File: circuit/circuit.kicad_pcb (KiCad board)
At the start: 2 copper layers, 25 parts, among them J1 JST-PH_2_RA, J2 CONN_02X03, U1 SK812, U2 MIC5504-3.3YM5, U3 ADXL345, U4 ATmega328-AU, Y1 Crystal_SMD

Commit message: modified schematic and layout:
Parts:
- removed J2: CONN_02X03, rocketry:Pin_Header_Straight_2x03
- added C8: C_1uF, footprints:C_0805_OEM, F.Cu at (187.8, 85.4)
- added C9: C_0.1uF, footprints:C_0805_OEM, F.Cu at (185.7, 85.4)
- added U5: USB_MicroB, Connectors_USB:USB_Micro-B_Molex-105017-0001, F.Cu at (189.3, 76.4)
- C2: value C_30pF -> C_10uF; footprint rocketry:C_0805_OEM -> footprints:C_0805_OEM
- C3: value C_30pF -> C_100uF; footprint rocketry:C_0805_OEM -> footprints:C_0805_OEM
- U2: value MIC5504-3.3YM5 -> LM1117-3.3; footprint rocketry:SOT-23-5_OEM -> TO_SOT_Packages_SMD:SOT-223
- moved D3 127.9 mm to (211.5, 80.8), turned to 90 degrees
- moved D2 123.2 mm to (205.2, 110.9), turned to 90 degrees
- moved D1 118.3 mm to (197.8, 76.2), turned to 180 degrees
- moved C2 117.6 mm to (209.5, 86.2), turned to 270 degrees
- moved C4 117.3 mm to (207.6, 98.8), turned to 90 degrees
- moved R3 114.5 mm to (211.6, 84.5), turned to 90 degrees
- moved R1 112.5 mm to (207.2, 111.3), turned to 270 degrees
- moved U1 111.4 mm to (188.0, 110.4), turned to 90 degrees
- moved U3 110.8 mm to (190.7, 86.4)
- moved C7 110.5 mm to (204.1, 102.6), turned to 90 degrees
- moved R2 109.5 mm to (197.8, 78.3), turned to 180 degrees
- moved C5 102.1 mm to (205.0, 95.4)
- moved C3 101.6 mm to (203.8, 92.5)
- moved Y1 101.4 mm to (204.9, 98.6), turned to 90 degrees
- moved R5 101.0 mm to (188.8, 106.0)
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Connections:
- C1 pad 1: GND -> VCC
- C3 pad 1: GND -> VCC
- C4 pad 2: Net-(C4-Pad2) -> GND
- C5 pad 2: Net-(C4-Pad2) -> GND
- C7 pad 2: GND -> VCC
- D3 pad 2: GND -> VCC
- R6 pad 2: GND -> VCC
- R7 pad 1: GND -> VCC
- SD1 pad 4: GND -> VCC
- U1 pad 1: GND -> VCC
- U2 pad 1: /Battery+ -> GND
- U2 pad 2: GND -> VCC
- U2 pad 4: Net-(U2-Pad4) -> VCC
- U3 pad 1: GND -> VCC
- U3 pad 6: GND -> VCC
- U4 pad 1: /INT2 -> Net-(U4-Pad1)
- U4 pad 11: Net-(U4-Pad11) -> /SD_Select
- U4 pad 12: /P_LED_1 -> /cardIN
- U4 pad 13: /cardIN -> /INT2
- U4 pad 14: Net-(U4-Pad14) -> /INT1
- U4 pad 25: /SD_Select -> Net-(U4-Pad25)
- U4 pad 27: Net-(U4-Pad27) -> /P_LED_1
- U4 pad 32: /INT1 -> Net-(U4-Pad32)
- U4 pad 4: GND -> VCC
- U4 pad 6: GND -> VCC
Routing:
- net GND: track 0.00 -> 66.0 mm, vias 0 -> 19
- net VCC: track 0.00 -> 64.5 mm, vias 0 -> 8
- net /miso: track 0.00 -> 33.8 mm, vias 0 -> 1
- net /mosi: track 0.00 -> 33.0 mm, vias 0 -> 6
- net /sck: track 0.00 -> 22.9 mm, vias 0 -> 3
- net /SD_Select: track 0.00 -> 19.8 mm, vias 0 -> 3
- net /Slave_Select: track 0.00 -> 18.8 mm
- net /P_LED_1: track 0.00 -> 12.6 mm
- net /INT2: track 0.00 -> 12.1 mm, vias 0 -> 2
- net /INT1: track 0.00 -> 10.6 mm, vias 0 -> 2
- net /Neopix: track 0.00 -> 7.33 mm
- net /Battery+: track 0.00 -> 5.59 mm
- net Net-(C4-Pad1): track 0.00 -> 4.82 mm
- net Net-(C6-Pad1): track 0.00 -> 3.94 mm
- net /cardIN: track 0.00 -> 2.79 mm
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- added copper zone on B.Cu, net GND
- added copper zone on F.Cu, net GND
- added copper zone on F.Cu, net VCC
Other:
- board outline added: 30 x 40 mm
- net class Default: clearance 0.2 -> 0.1524; trace_width 0.25 -> 0.1524; via_dia 0.8 -> 0.6096; via_drill 0.4 -> 0.3048
- rule trace_clearance: 0.2 -> 0.1524
- rule trace_min: 0.2 -> 0.1524
- rule via_min_drill: 0.3 -> 0.3048
- rule via_min_size: 0.4 -> 0.6096
- board text added: "PLUG IN SD"

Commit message: did some more work on the layout. added some graphics
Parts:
- added G***: LOGO, rocketry:pigeon, B.Cu at (198.4, 102.5)
- moved R4 0.55 mm to (197.5, 92.9)
- renumbered U5 to J5
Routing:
- net VCC: track 64.5 -> 128.9 mm, vias 8 -> 18
- net /RESET: track 2.37 -> 41.0 mm, vias 0 -> 2
- net /cardIN: track 2.79 -> 22.7 mm, vias 0 -> 3
- net GND: track 66.0 -> 75.9 mm, vias 19 -> 22
- net /sck: track 22.9 -> 32.3 mm, vias 3 -> 5
- net Net-(C5-Pad1): track 2.38 -> 4.53 mm
- net Net-(D1-Pad2): track 0.00 -> 2.11 mm
- net Net-(C4-Pad1): track 4.82 -> 6.82 mm
- net /miso: track 33.8 -> 32.1 mm, vias 1 -> 3
- net /mosi: track 33.0 -> 32.1 mm, vias 6 -> 4
- net /Slave_Select: track 18.8 -> 18.1 mm
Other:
- board text added: "REV - 1 - 2019"
- board text added: "WF AB SB"

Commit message: revision two
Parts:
- removed J5: USB_MicroB, Connectors_USB:USB_Micro-B_Molex-105017-0001
- added R10: R_4.7K, footprints:R_0805_OEM, F.Cu at (197.6, 86.9)
- added R11: R_10K, footprints:R_0805_OEM, F.Cu at (210.8, 91.4)
- added R8: R_4.7K, footprints:R_0805_OEM, F.Cu at (195.5, 86.9)
- added R9: R_10K, footprints:R_0805_OEM, F.Cu at (200.2, 95.6)
- added U5: USB_MicroB, Connectors_USB:USB_Micro-B_Molex-105017-0001, F.Cu at (189.3, 76.4)
- added U6: 4050_Logic_Buffer, Housings_SOIC:SOIC-16_3.9x9.9mm_Pitch1.27mm, F.Cu at (188.6, 92.1)
- C2: value C_10uF -> C_0.1uF
- C3: value C_100uF -> C_1uF
- U2: value LM1117-3.3 -> TCR2EF33LM; footprint TO_SOT_Packages_SMD:SOT-223 -> rocketry:SOT25
- moved C9 17.5 mm to (201.6, 92.8)
- moved U3 16.1 mm to (205.2, 93.5)
- moved C8 13.9 mm to (199.6, 92.8)
- moved R4 10.8 mm to (200.9, 82.7)
- moved C1 8.34 mm to (186.1, 111.6), turned to 90 degrees
- moved R7 7.24 mm to (191.4, 103.8)
- moved C3 6.87 mm to (199.8, 86.9), turned to 90 degrees
- moved C6 4.51 mm to (193.4, 104.0)
- moved C4 4.31 mm to (209.9, 102.5)
- moved R6 4.31 mm to (201.6, 110.9)
- moved Y1 4.31 mm to (207.1, 102.3)
- moved C7 4.31 mm to (206.3, 106.3)
- moved C5 4.31 mm to (207.2, 99.1)
- moved U4 4.31 mm to (199.8, 104.4)
- moved C2 4.18 mm to (205.4, 86.9), turned to 90 degrees
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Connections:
- C1 pad 1: VCC -> /Battery+
- C7 pad 2: VCC -> /Battery+
- R6 pad 2: VCC -> /Battery+
- R7 pad 1: VCC -> /Battery+
- SD1 pad 2: /SD_Select -> /SD_CS_3V
- SD1 pad 3: /mosi -> /MOSI_3V
- SD1 pad 5: /sck -> /SCK_3V
- SD1 pad 7: /miso -> /MISO_3V
- U1 pad 1: VCC -> GND
- U1 pad 3: GND -> /Battery+
- U2 pad 1: GND -> /Battery+
- U2 pad 2: VCC -> GND
- U2 pad 4: VCC -> Net-(U2-Pad4)
- U3 pad 12: /mosi -> Net-(R11-Pad1)
- U3 pad 13: /miso -> /SDA_3V
- U3 pad 14: /sck -> /SCL_3V
- U3 pad 7: /Slave_Select -> Net-(R9-Pad2)
- U4 pad 11: /SD_Select -> /SD_CS
- U4 pad 15: /mosi -> /MOSI
- U4 pad 16: /miso -> /MISO
- U4 pad 17: /sck -> /SCK
- U4 pad 24: /Slave_Select -> /P_LED_1
- U4 pad 27: /P_LED_1 -> /SDA
- U4 pad 28: Net-(U4-Pad28) -> /SCL
- U4 pad 4: VCC -> /Battery+
- U4 pad 6: VCC -> /Battery+
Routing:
- net /Battery+: track 5.59 -> 98.6 mm, vias 0 -> 6
- net VCC: track 128.9 -> 71.6 mm, vias 18 -> 10
- net /SCK: track 0.00 -> 35.3 mm, vias 0 -> 2
- net /MISO: track 0.00 -> 34.2 mm, vias 0 -> 2
- net /MOSI: track 0.00 -> 33.6 mm
- net /sck: track 32.3 -> 0.00 mm, vias 5 -> 0
- net /mosi: track 32.1 -> 0.00 mm, vias 4 -> 0
- net /miso: track 32.1 -> 0.00 mm, vias 3 -> 0
- net /SCK_3V: track 0.00 -> 26.5 mm, vias 0 -> 3
- net /MISO_3V: track 0.00 -> 26.3 mm, vias 0 -> 3
- net /SCL: track 0.00 -> 24.1 mm, vias 0 -> 2
- net /SDA_3V: track 0.00 -> 21.8 mm, vias 0 -> 2
- net /SD_CS_3V: track 0.00 -> 21.5 mm, vias 0 -> 1
- net /SDA: track 0.00 -> 20.7 mm, vias 0 -> 2
- net /SCL_3V: track 0.00 -> 20.1 mm, vias 0 -> 3
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- removed copper zone on F.Cu, net VCC
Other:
- board text added: "ADR"
- board text added: "REV - 2 - 2019"
- board text removed: "REV - 1 - 2019"

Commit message: starting rev 3
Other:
- board text added: "REV - 3 - 2019"
- board text removed: "REV - 2 - 2019"
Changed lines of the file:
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@@
     (effects (font (size 1.5 0.8) (thickness 0.2)))
   )
-  (gr_text "REV - 2 - 2019" (at 198.15 112.58) (layer B.SilkS)
+  (gr_text "REV - 3 - 2019" (at 198.15 112.58) (layer B.SilkS)
     (effects (font (size 1.5 1.5) (thickness 0.3)) (justify mirror))
   )

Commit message: working on rev3
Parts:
- removed G***: LOGO, rocketry:pigeon
- removed R10: R_4.7K, footprints:R_0805_OEM
- removed U6: 4050_Logic_Buffer, Housings_SOIC:SOIC-16_3.9x9.9mm_Pitch1.27mm
- C2: value C_0.1uF -> C_10uF
- C3: value C_1uF -> C_10uF
- R4: footprint rocketry:R_0805_OEM -> footprints:R_0805_OEM
- R8: value R_4.7K -> R_10K
- SD1: value Micro_SD_Card_A118117CT-ND -> MicroSD_V2; footprint rocketry:Micro_SD_Card_A118117CT-ND -> rocketry:Micro_SD_Card_Holder_Molex
- U2: value TCR2EF33LM -> LM1117MPX-3.3; footprint rocketry:SOT25 -> TO_SOT_Packages_SMD:SOT-223
- moved R11 24.1 mm to (186.7, 90.3)
- moved R4 15.3 mm to (193.9, 96.2)
- moved R9 14.8 mm to (189.7, 85.1), turned to 270 degrees
- moved U3 13.2 mm to (192.3, 91.1), turned to 180 degrees
- moved SD1 12.7 mm to (192.3, 90.4)
- moved C9 11.5 mm to (193.0, 85.2)
- moved R8 9.95 mm to (188.6, 94.1), turned to 90 degrees
- moved C8 8.47 mm to (195.9, 85.2)
- moved U2 5.79 mm to (204.3, 92.3), turned to 180 degrees
- moved C3 3.69 mm to (200.2, 83.2)
- moved C2 1.23 mm to (206.4, 86.2), turned to 180 degrees
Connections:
- C1 pad 1: /Battery+ -> VCC
- C7 pad 2: /Battery+ -> VCC
- R2 pad 1: /cardIN -> /Dectect_LED
- R4 pad 1: /cardIN -> VCC
- R4 pad 2: GND -> /SCL
- R6 pad 2: /Battery+ -> VCC
- R7 pad 1: /Battery+ -> VCC
- R8 pad 2: /SCL_3V -> /SDA
- SD1 pad 2: /SD_CS_3V -> /SD_CS
- SD1 pad 3: /MOSI_3V -> /MOSI
- SD1 pad 5: /SCK_3V -> /SCK
- SD1 pad 7: /MISO_3V -> /MISO
- SD1 pad 9: VCC -> /Dectect_LED
- U1 pad 3: /Battery+ -> VCC
- U2 pad 1: /Battery+ -> GND
- U2 pad 2: GND -> VCC
- U2 pad 4: Net-(U2-Pad4) -> VCC
- U3 pad 13: /SDA_3V -> /SDA
- U3 pad 14: /SCL_3V -> /SCL
- U4 pad 12: /cardIN -> /Dectect_LED
- U4 pad 4: /Battery+ -> VCC
- U4 pad 6: /Battery+ -> VCC
- U5 pad 1: /Battery+ -> VCC
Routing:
- net /Battery+: track 98.6 -> 0.00 mm, vias 6 -> 0
- net /RESET: track 43.7 -> 3.11 mm, vias 2 -> 0
- net /cardIN: track 39.1 -> 0.00 mm, vias 12 -> 0
- net /SCK: track 35.3 -> 0.00 mm, vias 2 -> 0
- net /MISO: track 34.2 -> 0.00 mm, vias 2 -> 0
- net /MOSI: track 33.6 -> 0.00 mm
- net /SCK_3V: track 26.5 -> 0.00 mm, vias 3 -> 0
- net /MISO_3V: track 26.3 -> 0.00 mm, vias 3 -> 0
- net GND: track 91.2 -> 69.0 mm, vias 26 -> 15
- net /SDA_3V: track 21.8 -> 0.00 mm, vias 2 -> 0
- net VCC: track 71.6 -> 93.0 mm, vias 10 -> 6
- net /SCL_3V: track 20.1 -> 0.00 mm, vias 3 -> 0
- net /SD_CS_3V: track 21.5 -> 2.42 mm, vias 1 -> 0
- net /MOSI_3V: track 18.1 -> 0.00 mm, vias 3 -> 0
- net /SD_CS: track 13.3 -> 0.00 mm, vias 4 -> 0
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
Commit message: Did some more vias and traces - I don't know if this board looks good
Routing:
- net GND: track 69.0 -> 123.7 mm, vias 15 -> 21
- net /RESET: track 3.11 -> 54.7 mm, vias 0 -> 2
- net VCC: track 93.0 -> 135.6 mm, vias 6 -> 11
- net /MISO: track 0.00 -> 39.0 mm, vias 0 -> 9
- net /MOSI: track 0.00 -> 33.4 mm, vias 0 -> 4
- net /INT2: track 0.00 -> 27.3 mm, vias 0 -> 2
- net /Dectect_LED: track 0.00 -> 25.8 mm, vias 0 -> 2
- net /INT1: track 0.00 -> 22.6 mm, vias 0 -> 2
- net /SD_CS: track 0.00 -> 21.5 mm, vias 0 -> 1
- net /SCK: track 0.00 -> 9.84 mm, vias 0 -> 1
- net /Battery+: track 0.00 -> 7.78 mm

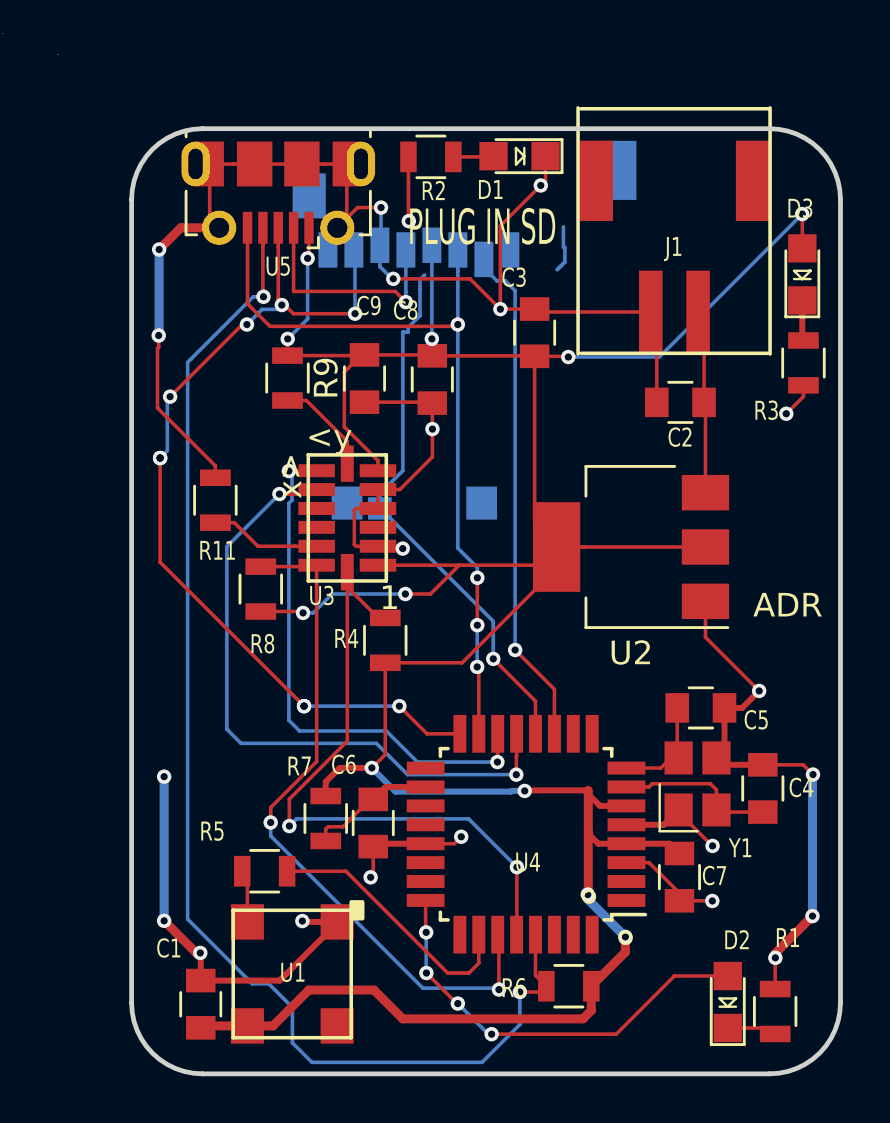
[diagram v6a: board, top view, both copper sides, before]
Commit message: Did some moving around of parts and made the layout cleaner. I think this looks better!
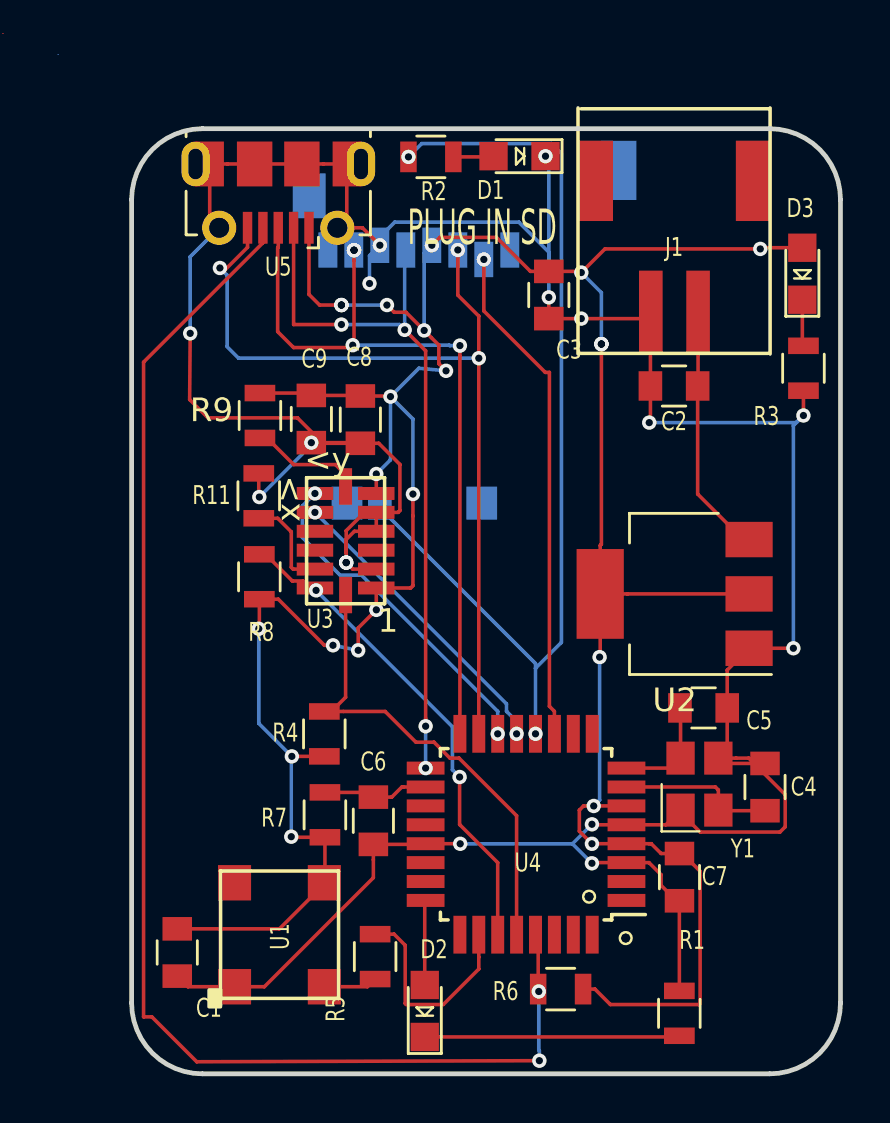
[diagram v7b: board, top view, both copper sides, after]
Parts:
- moved D2 12.8 mm to (195.6, 111.9)
- moved R5 5.91 mm to (193.4, 109.6), turned to 90 degrees
- moved R4 4.73 mm to (191.3, 100.2)
- moved R1 4.06 mm to (206.3, 112.0)
- moved U1 3.65 mm to (191.3, 108.7), turned to 270 degrees
- moved C8 3.49 mm to (192.8, 86.9)
- moved C9 2.83 mm to (190.8, 86.9)
- moved U2 2.71 mm to (206.1, 94.3)
- moved C1 2.41 mm to (185.1, 109.5), turned to 270 degrees
- moved R9 1.97 mm to (188.6, 86.7)
- moved R11 1.84 mm to (188.5, 90.1)
- moved C3 1.70 mm to (200.8, 81.6), turned to 270 degrees
- moved U3 0.97 mm to (192.2, 92.0)
- moved C2 0.75 mm to (206.1, 85.5)
- moved R8 0.52 mm to (188.6, 93.5)
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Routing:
- net GND: track 123.7 -> 147.2 mm, vias 21 -> 16
- net /SCK: track 9.84 -> 31.3 mm, vias 1 -> 4
- net /Dectect_LED: track 25.8 -> 41.4 mm
- net /INT2: track 27.3 -> 12.9 mm
- net /P_LED_1: track 17.9 -> 3.59 mm, vias 4 -> 0
- net Net-(D2-Pad1): track 2.11 -> 10.8 mm
- net /SDA: track 29.4 -> 20.7 mm
- net /INT1: track 22.6 -> 14.3 mm
- net /SCL: track 28.0 -> 20.5 mm, vias 2 -> 0
- net /MISO: track 39.0 -> 33.1 mm, vias 9 -> 4
- net /MOSI: track 33.4 -> 37.6 mm, vias 4 -> 3
- net /RESET: track 54.7 -> 58.4 mm
- net /Battery+: track 7.78 -> 10.7 mm
- net /SD_CS_3V: track 2.42 -> 0.00 mm
- net /Neopix: track 11.3 -> 9.14 mm
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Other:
- board text removed: "ADR"

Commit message: Latest updates to the PCB design
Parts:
- moved C3 15.1 mm to (208.2, 94.8), turned to 0 degrees
- moved C9 6.01 mm to (195.6, 90.4)
- moved C8 5.87 mm to (197.5, 90.4)
- moved C1 4.75 mm to (188.5, 112.8), turned to 180 degrees
- moved U2 4.52 mm to (208.0, 90.2)
- moved SD1 4.34 mm to (196.6, 90.7)
- moved R9 2.66 mm to (191.1, 87.6), turned to 180 degrees
- moved R8 2.65 mm to (186.7, 95.4)
- moved R11 2.65 mm to (187.7, 87.6), turned to 180 degrees
- moved D3 1.99 mm to (211.6, 78.7)
- moved C2 1.93 mm to (208.0, 85.6)
- moved R3 0.91 mm to (211.6, 83.8)
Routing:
- net GND: track 147.2 -> 90.0 mm, vias 16 -> 18
- net /INT2: track 12.9 -> 29.4 mm, vias 2 -> 4
- net /INT1: track 14.3 -> 29.5 mm, vias 2 -> 4
- net /Battery+: track 10.7 -> 0.00 mm
- net /RESET: track 58.4 -> 48.7 mm
- net VCC: track 133.7 -> 125.7 mm, vias 22 -> 17
- net /Dectect_LED: track 41.4 -> 35.0 mm, vias 2 -> 1
- net /SCK: track 31.3 -> 37.5 mm, vias 4 -> 1
- net /MISO: track 33.1 -> 38.9 mm, vias 4 -> 5
- net /SDA: track 20.7 -> 24.2 mm, vias 2 -> 4
- net Net-(R11-Pad1): track 4.15 -> 7.59 mm, vias 0 -> 2
- net /MOSI: track 37.6 -> 40.7 mm, vias 3 -> 5
- net /Neopix: track 9.14 -> 6.16 mm, vias 0 -> 2
- net Net-(R9-Pad2): track 4.77 -> 3.24 mm
- net Net-(D3-Pad1): track 1.97 -> 3.03 mm
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- added copper zone on F.Cu, net /Battery+
